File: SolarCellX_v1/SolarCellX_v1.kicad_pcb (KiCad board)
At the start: 2 copper layers, 48 x 48 mm, 12 parts

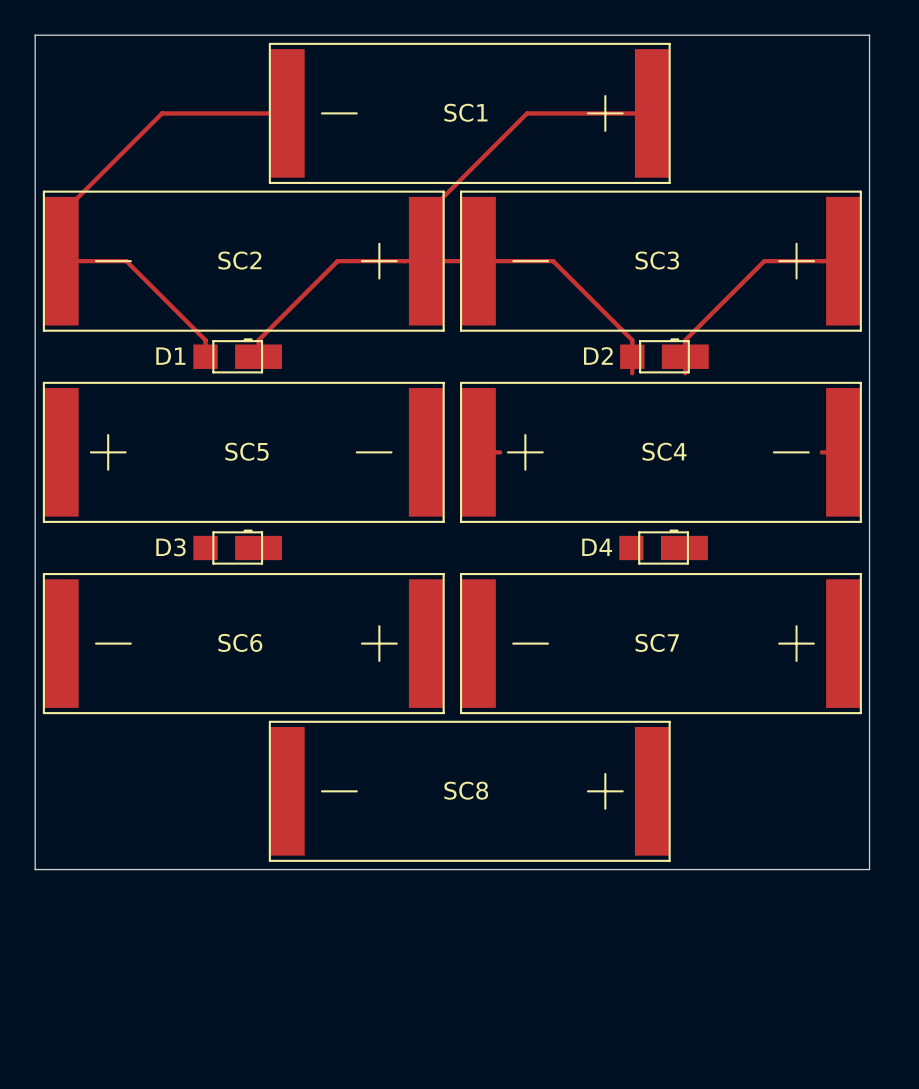
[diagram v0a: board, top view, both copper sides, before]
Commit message: Finished the trace layout
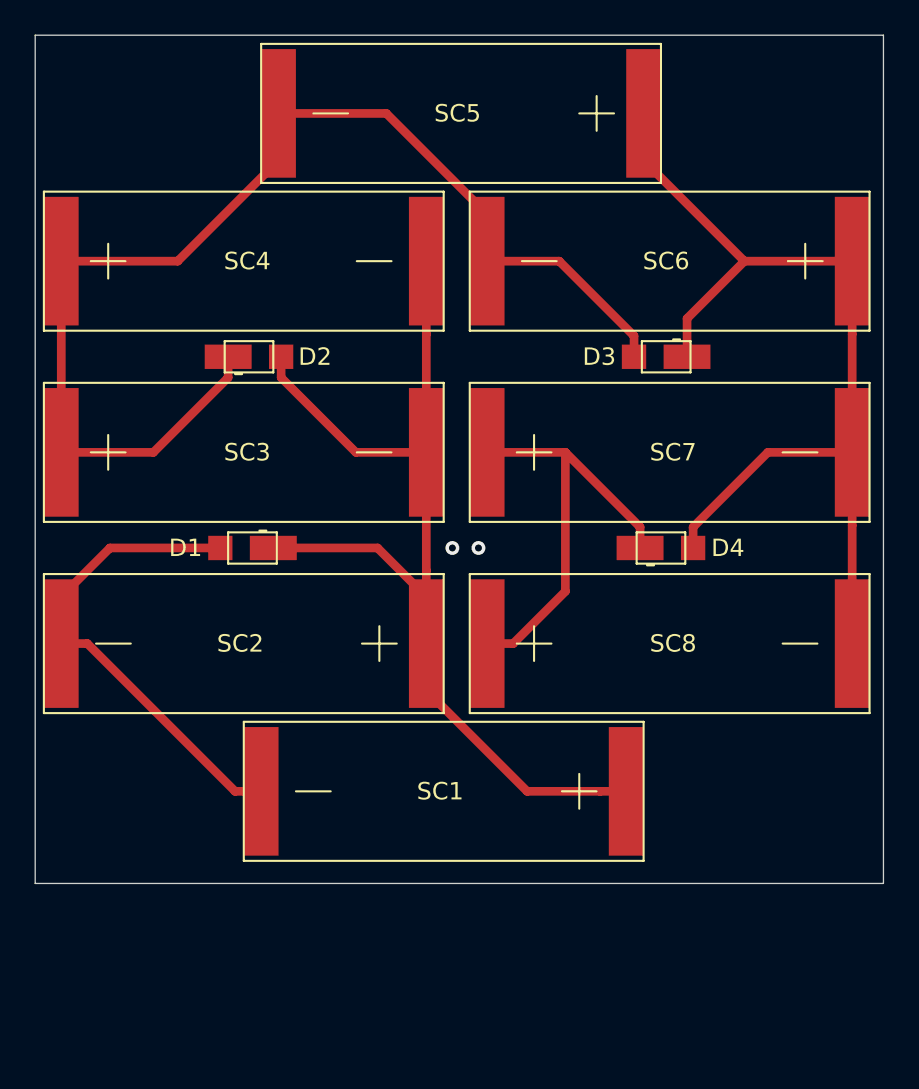
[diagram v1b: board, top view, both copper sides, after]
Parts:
- moved SC3 46.3 mm to (91.5, 64.0), turned to 0 degrees
- moved SC1 39.0 mm to (124.0, 83.5)
- moved SC5 38.8 mm to (125.0, 44.5), turned to 180 degrees
- moved SC6 32.9 mm to (137.0, 53.0)
- moved D3 27.0 mm to (126.3, 58.5)
- moved SC4 26.4 mm to (91.5, 53.0)
- moved D2 23.9 mm to (102.3, 58.5), turned to 0 degrees
- moved SC7 23.3 mm to (116.0, 64.0), turned to 0 degrees
- moved SC2 22.0 mm to (112.5, 75.0)
- moved SC8 12.7 mm to (116.0, 75.0), turned to 0 degrees
- moved D1 11.0 mm to (102.5, 69.5)
- moved D4 0.15 mm to (126.0, 69.5), turned to 0 degrees
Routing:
- net Net-(D3-Pad1): track 0.00 -> 58.1 mm
- net Net-(D2-Pad1): track 14.1 -> 69.7 mm
- net Net-(D4-Pad1): track 0.00 -> 25.5 mm
- net Net-(D1-Pad1): track 47.5 -> 62.6 mm
- net Net-(D1-Pad2): track 29.2 -> 28.0 mm
- net (no net): vias 0 -> 2
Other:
- board size 48 x 48 mm -> 48.8 x 48.8 mm
- copper layers 2 -> 6

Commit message: Added the mounting & USB hole
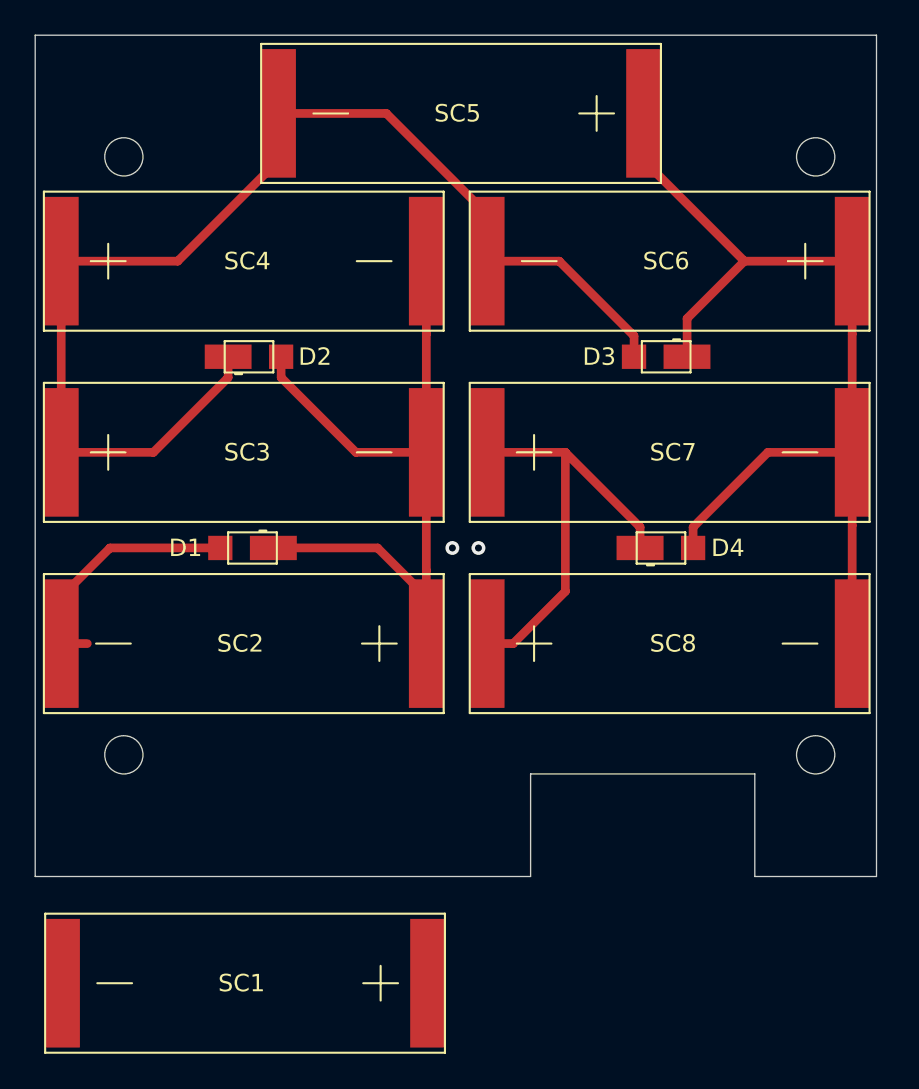
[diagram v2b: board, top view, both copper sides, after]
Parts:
- moved SC1 15.9 mm to (112.6, 94.5)
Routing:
- net Net-(D1-Pad1): track 62.6 -> 48.7 mm
- net Net-(D1-Pad2): track 28.0 -> 14.5 mm
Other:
- board size 48.8 x 48.8 mm -> 48.4 x 48.4 mm
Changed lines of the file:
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@@
   (general
     (thickness 1.6)
-    (drawings 4)
-    (tracks 53)
+    (drawings 12)
+    (tracks 48)
     (zones 0)
     (modules 12)
@@
   )
   (setup
-    (last_trace_width 0.5)
+    (last_trace_width 0.25)
+    (user_trace_width 0.127)
     (user_trace_width 0.5)
     (user_trace_width 1)
@@
   )
   (module SolarCellX:KXOB25-05X3F (layer F.Cu)
-    (at 124 83.5 180)
+    (at 112.5728 94.5388 180)
     (fp_text reference SC1 (at 10.7 0) (layer F.SilkS)
       (effects (font (size 1 1) (thickness 0.15)))
@@
       (net 4 "Net-(D3-Pad1)"))
   )
-  (gr_line (start 138.8 88.8) (end 90 88.8) (layer Edge.Cuts) (width 0.05))
-  (gr_line (start 90 88.8) (end 90 40) (layer Edge.Cuts) (width 0.05))
-  (gr_line (start 138.8 40) (end 138.8 88.8) (layer Edge.Cuts) (width 0.05))
-  (gr_line (start 90 40) (end 138.8 40) (layer Edge.Cuts) (width 0.05))
+  (gr_line (start 138.4 88.4) (end 131.4 88.4) (layer Edge.Cuts) (width 0.05))
+  (gr_line (start 131.4 88.4) (end 131.4 82.5) (layer Edge.Cuts) (width 0.05))
+  (gr_line (start 131.4 82.5) (end 118.5 82.5) (layer Edge.Cuts) (width 0.05))
+  (gr_line (start 118.5 82.5) (end 118.5 88.4) (layer Edge.Cuts) (width 0.05))
+  (gr_circle (center 95.1 81.4) (end 96.2 81.4) (layer Edge.Cuts) (width 0.05))
+  (gr_circle (center 134.9 81.4) (end 136 81.4) (layer Edge.Cuts) (width 0.05))
+  (gr_circle (center 134.9 47) (end 136 47) (layer Edge.Cuts) (width 0.05))
+  (gr_circle (center 95.1 47) (end 96.2 47) (layer Edge.Cuts) (width 0.05))
+  (gr_line (start 118.5 88.4) (end 90 88.4) (layer Edge.Cuts) (width 0.05))
+  (gr_line (start 90 88.4) (end 90 40) (layer Edge.Cuts) (width 0.05))
+  (gr_line (start 138.4 40) (end 138.4 88.4) (layer Edge.Cuts) (width 0.05))
+  (gr_line (start 90 40) (end 138.4 40) (layer Edge.Cuts) (width 0.05))
   (via (at 114 69.5) (size 0.8) (drill 0.4) (layers F.Cu B.Cu) (net 0))
   (via (at 115.5 69.5) (size 0.8) (drill 0.4) (layers F.Cu B.Cu) (net 0))
-  (segment (start 101.5 83.5) (end 103 83.5) (width 0.5) (layer F.Cu) (net 1))
-  (segment (start 93 75) (end 101.5 83.5) (width 0.5) (layer F.Cu) (net 1))
   (segment (start 91.5 75) (end 93 75) (width 0.5) (layer F.Cu) (net 1))
   (segment (start 91.5 72.3) (end 91.5 75) (width 0.5) (layer F.Cu) (net 1))
   (segment (start 94.3 69.5) (end 91.5 72.3) (width 0.5) (layer F.Cu) (net 1))
   (segment (start 100.65 69.5) (end 94.3 69.5) (width 0.5) (layer F.Cu) (net 1))
-  (segment (start 122.5 83.5) (end 124 83.5) (width 0.5) (layer F.Cu) (net 2))
-  (segment (start 118.3 83.5) (end 122.5 83.5) (width 0.5) (layer F.Cu) (net 2))
-  (segment (start 112.5 77.7) (end 118.3 83.5) (width 0.5) (layer F.Cu) (net 2))
   (segment (start 112.5 75) (end 112.5 77.7) (width 0.5) (layer F.Cu) (net 2))
   (segment (start 112.5 72.3) (end 112.5 75) (width 0.5) (layer F.Cu) (net 2))
